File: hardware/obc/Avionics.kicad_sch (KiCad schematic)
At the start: 44 parts, among them J1 Conn_02x20_Odd_Even, U1 MAX706RESA, U2 ATSAMD51J20A-AU, U3 BMI088, Y1 32.768kHz

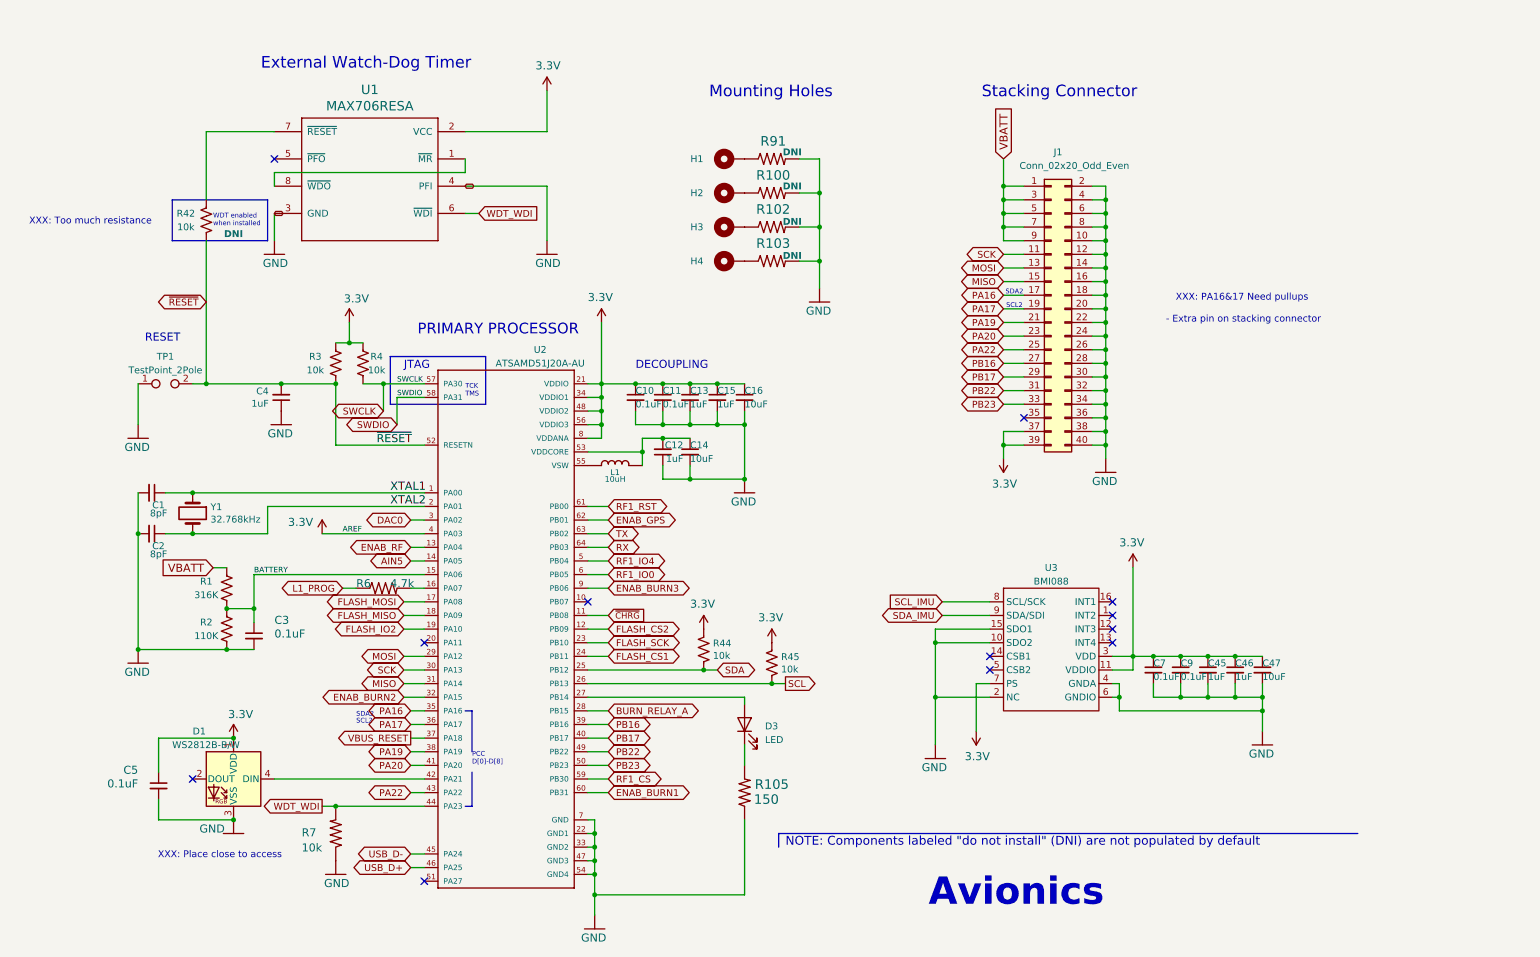
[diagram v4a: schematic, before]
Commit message: obc: BOM component verification
Verified part numbers, availability, values, footprints, etc. of components. Next steps involve verifying footprints and potentially researching some alternative components.
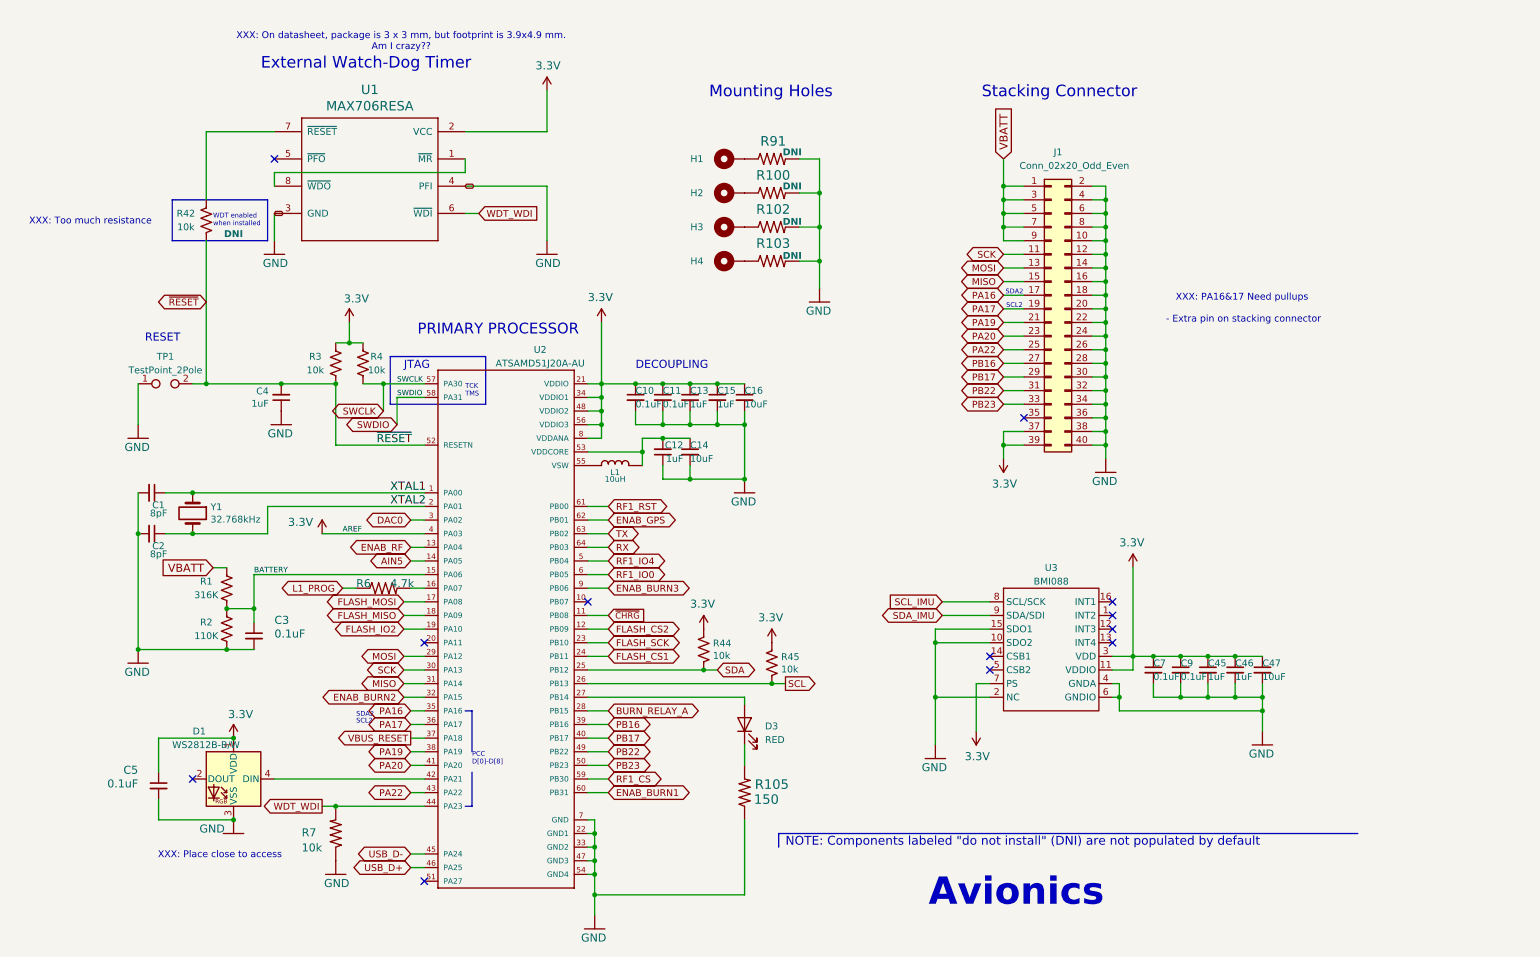
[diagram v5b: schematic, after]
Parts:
- C1, C2: LCSC C346204 -> C1882476; Manufacturer_Name Samsung Electro-Mechanics -> YAGEO; Manufacturer_Part_Number CL10C080DB81PNC -> CC0603JRNPO9BN8R0
- C12, C13, C15, C4, C45, C46: Manufacturer_Name (none) -> Samsung Electro-Mechanics; Manufacturer_Part_Number (none) -> CL10B105KO8NNNC; Notes (none) -> 16V ok?
- C14, C16, C47: Notes (none) -> 10V ok?
- D3: value LED -> RED
- L1: Notes Processor Core V, Slightly sketchy vendor -> Footprint Marked as Issue - Processor Core V, Slightly sket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
- R100, R102, R103, R91: footprint (none) -> Resistor_SMD:R_0603_1608Metric
- U2: Notes (none) -> Consigned parts to JLCPCB.
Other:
- note added: "XXX: On datasheet, package is 3 x 3 mm, but footprint is 3.9x4.9 mm. Am I crazy??"

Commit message: obc: footprint editing and schematic revision
Added GPS21+ and edited inductor footprints. Edited schematic circuitry and re-annotated schematic components.
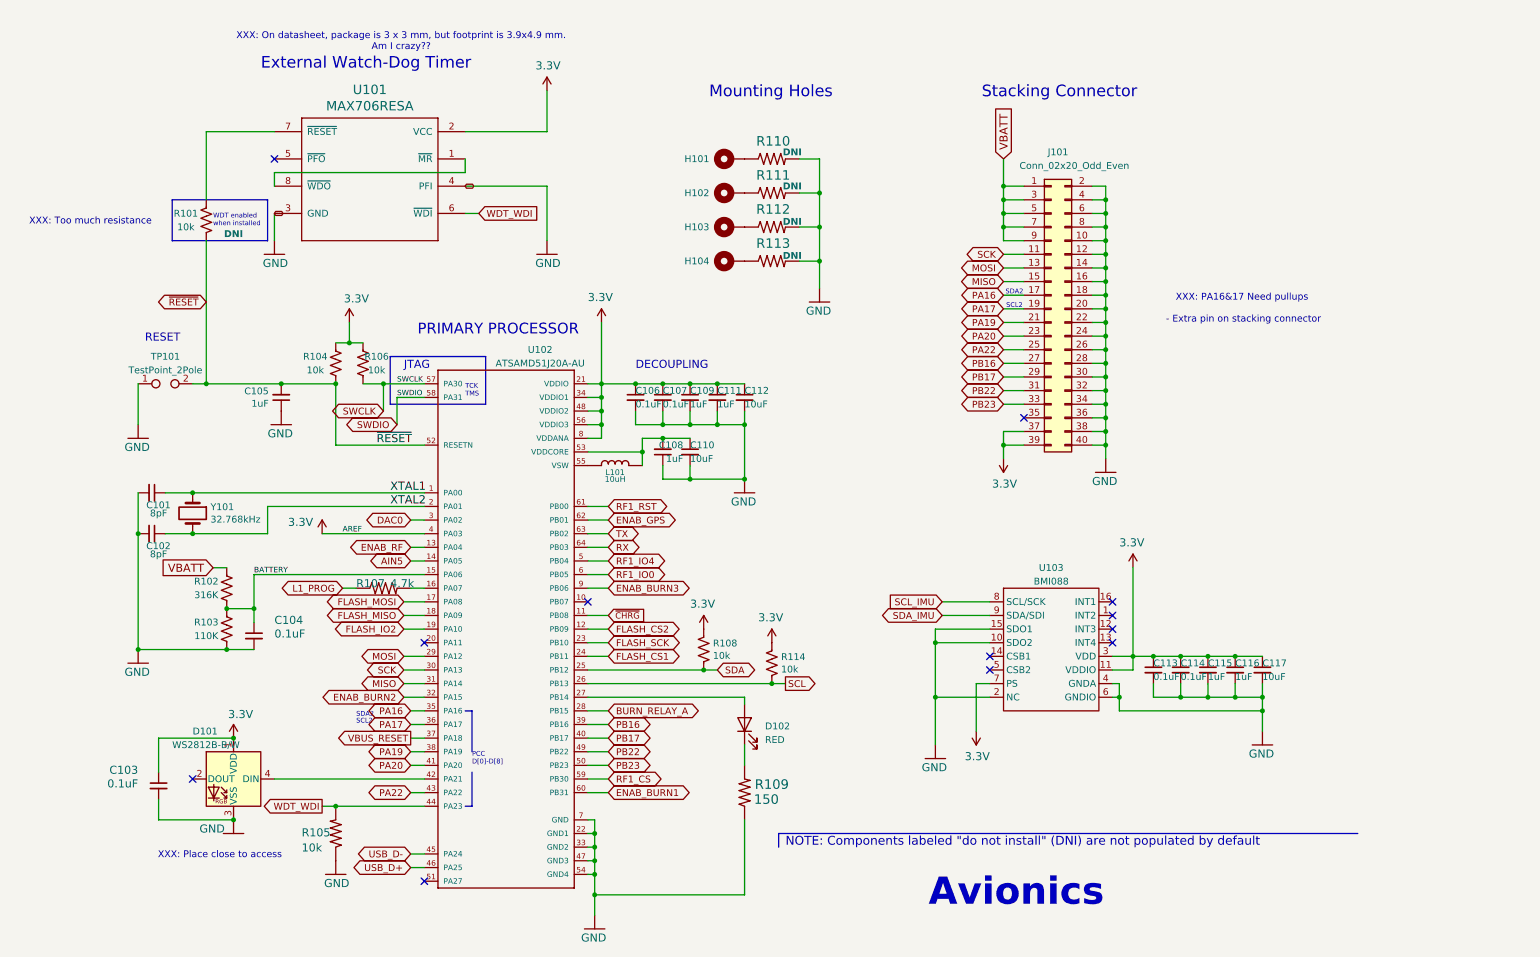
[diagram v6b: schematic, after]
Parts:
- J101: renamed from J1; footprint (none) -> Connector_PinHeader_2.54mm:PinHeader_2x20_P2.54mm_Vertical
- L101: renamed from L1; footprint SSE_Footprints:Sunlord_0805_2.0x1.6mm -> SSE_Footprints:Sunlord_0805_3.0x3.0mm
- R110: renamed from R91; value NA -> DNI
- R111: renamed from R100; value NA -> DNI
- R112: renamed from R102; value NA -> DNI
- R113: renamed from R103; value NA -> DNI
- renumbered C1 to C101, C2 to C102, C5 to C103, C3 to C104, C4 to C105, C10 to C106, C11 to C107, C12 to C108, C13 to C109, C14 to C110, C15 to C111, C16 to C112, C7 to C113, C9 to C114, C45 to C115, C46 to C116, C47 to C117, D1 to D101, D3 to D102, H1 to H101, H2 to H102, H3 to H103, H4 to H104, R42 to R101, R1 to R102, R2 to R103, R3 to R104, R7 to R105, R4 to R106, R6 to R107, R44 to R108, R105 to R109, R45 to R114, TP1 to TP101, U1 to U101, U2 to U102, U3 to U103, Y1 to Y101

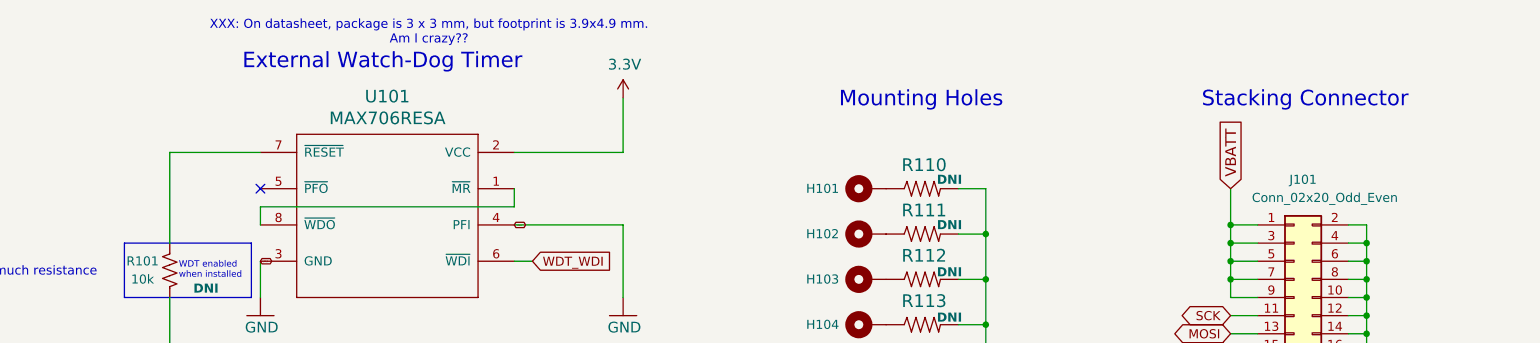
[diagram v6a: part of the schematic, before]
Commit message: obc: BOM editing
Edited the DNI status of several components to be more reflective of our obc setup plans.
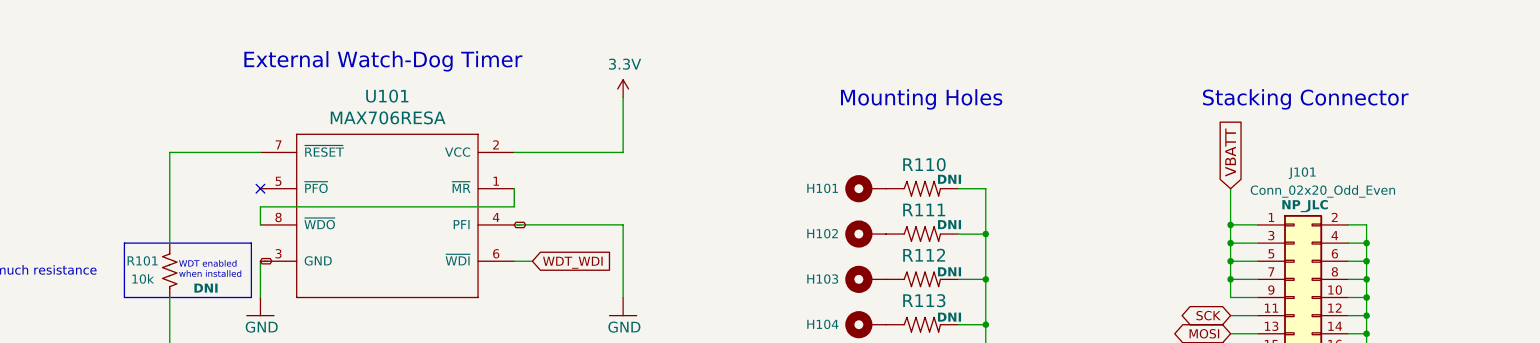
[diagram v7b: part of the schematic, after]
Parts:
- J101: DNI (none) -> NP_JLC
- R110, R111, R112, R113: Notes (none) -> Between mounting hole and ground.
- U102: Notes Consigned parts to JLCPCB. -> (none)
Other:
- note removed: "XXX: On datasheet, package is 3 x 3 mm, but footprint is 3.9x4.9 mm. Am I crazy??"
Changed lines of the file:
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@@
 		)
 	)
-	(text "XXX: On datasheet, package is 3 x 3 mm, but footprint is 3.9x4.9 mm. \nAm I crazy??"
-		(exclude_from_sim no)
-		(at 88.392 21.336 0)
-		(effects
-			(font
-				(size 1.27 1.27)
-			)
-		)
-	)
 	(label "XTAL1"
 		(at 86.36 105.41 0)
@@
 			)
 		)
-		(property "Notes" "Consigned parts to JLCPCB."
+		(property "Notes" ""
 			(at 107.95 130.81 0)
 			(effects
@@
 			)
 		)
-		(property "Description" ""
+		(property "Description" "Mounting Hole Pad"
 			(at 149.86 43.18 0)
 			(effects
@@
 			)
 		)
-		(property "Description" ""
+		(property "Description" "Mounting Hole Pad"
 			(at 149.86 49.53 0)
 			(effects
@@
 			)
 		)
-		(property "Description" ""
+		(property "Description" "Mounting Hole Pad"
 			(at 149.86 55.88 0)
 			(effects
@@
 			)
 		)
-		(property "Description" ""
+		(property "Description" "Mounting Hole Pad"
 			(at 149.86 62.23 0)
 			(effects
@@
 			)
 		)
-		(property "Description" ""
+		(property "Description" "0603"
 			(at 157.48 43.18 0)
 			(effects
@@
 			)
 		)
+		(property "Notes" "Between mounting hole and ground."
+			(at 157.48 43.18 0)
+			(effects
+				(font
+					(size 1.27 1.27)
+				)
+				(hide yes)
+			)
+		)
 		(pin "1"
 		)
@@
 		(dnp no)
 		(property "Reference" "J101"
-			(at 210.82 41.91 0)
+			(at 210.82 40.894 0)
 			(effects
 				(font
@@
 		)
 		(property "Value" "Conn_02x20_Odd_Even"
-			(at 213.868 44.45 0)
+			(at 213.614 43.434 0)
 			(effects
 				(font
@@
 			)
 		)
+		(property "DNI" "NP_JLC"
+			(at 211.074 45.466 0)
+			(effects
+				(font
+					(size 1.27 1.27)
+					(bold yes)
+				)
+			)
+		)
 		(pin "1"
 		)
@@
 			)
 		)
-		(property "Description" ""
+		(property "Description" "0603"
 			(at 157.48 49.53 0)
 			(effects
@@
 			)
 		)
+		(property "Notes" "Between mounting hole and ground."
+			(at 157.48 49.53 0)
+			(effects
+				(font
+					(size 1.27 1.27)
+				)
+				(hide yes)
+			)
+		)
 		(pin "1"
 		)
@@
 			)
 		)
-		(property "Description" ""
+		(property "Description" "0603"
 			(at 157.48 55.88 0)
 			(effects
@@
 			)
 		)
+		(property "Notes" "Between mounting hole and ground."
+			(at 157.48 55.88 0)
+			(effects
+				(font
+					(size 1.27 1.27)
+				)
+				(hide yes)
+			)
+		)
 		(pin "1"
 		)
@@
 			)
 		)
-		(property "Description" ""
+		(property "Description" "0603"
 			(at 157.48 62.23 0)
 			(effects
@@
 			(at 157.48 62.23 0)
 			(effects
+				(font
+					(size 1.27 1.27)
+				)
+				(hide yes)
+			)
+		)
+		(property "Notes" "Between mounting hole and ground."
+			(at 157.48 62.23 0)
+			(effects

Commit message: obc: preliminary board layout
Entered design rules and grouped components according to schematic. Slightly edited BOM.
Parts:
- U102: footprint mainboard:QFP50P1200X1200X120-64N -> Package_QFP:TQFP-64_10x10mm_P0.5mm
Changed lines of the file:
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@@
 			)
 		)
-		(property "Footprint" "mainboard:QFP50P1200X1200X120-64N"
+		(property "Footprint" "Package_QFP:TQFP-64_10x10mm_P0.5mm"
 			(at 107.95 130.81 0)
 			(effects
